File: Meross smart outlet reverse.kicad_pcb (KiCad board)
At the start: 2 copper layers, 60 x 33 mm, 61 parts, among them CN1 Conn_01x01, CN2 Conn_01x01, K1 HF32FV-16/5-HLTF(590), Q1 MMBT3904, SW1 SW_SPST, U1 OB2222M, U2 STK17-3.3, U3 CSE7759B

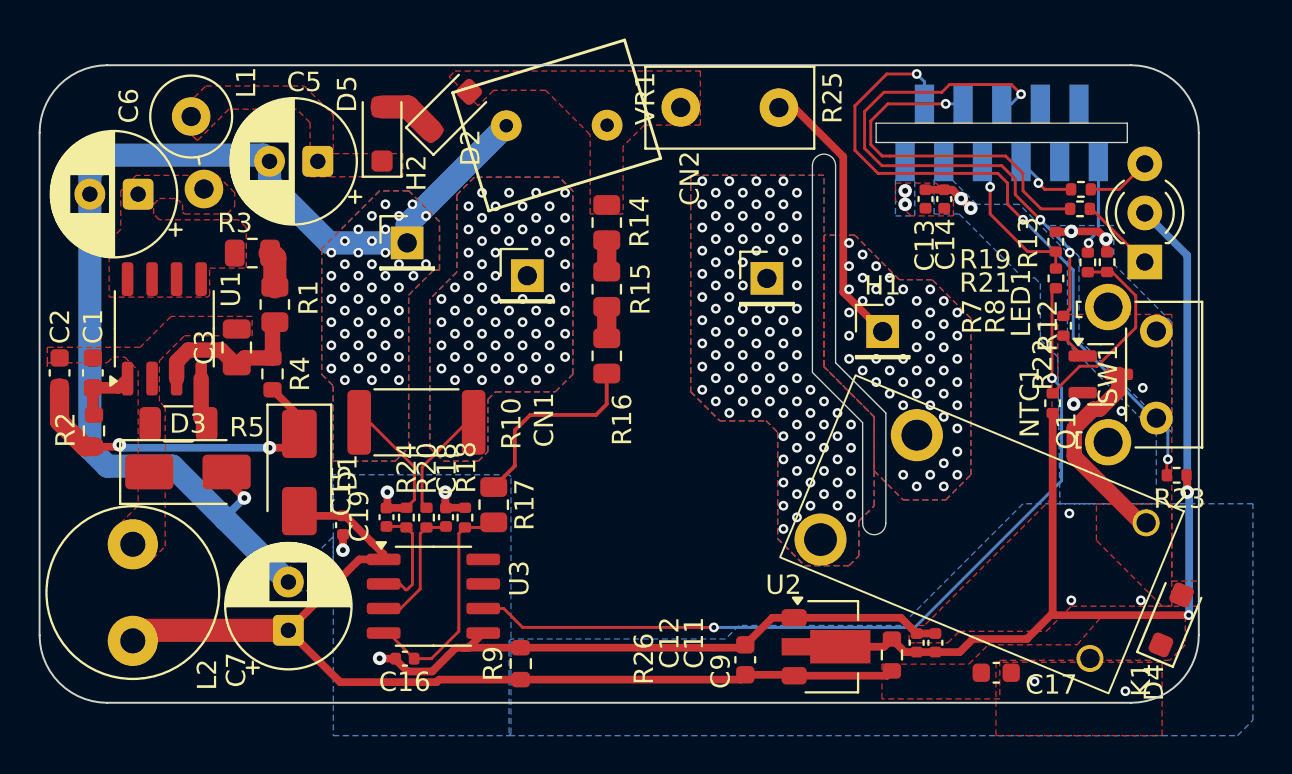
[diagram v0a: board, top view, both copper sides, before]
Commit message: Fixed plug and receptacle foots. No components left to fix but L1? And the silk and fab layers. And some kind of labeling of the design.
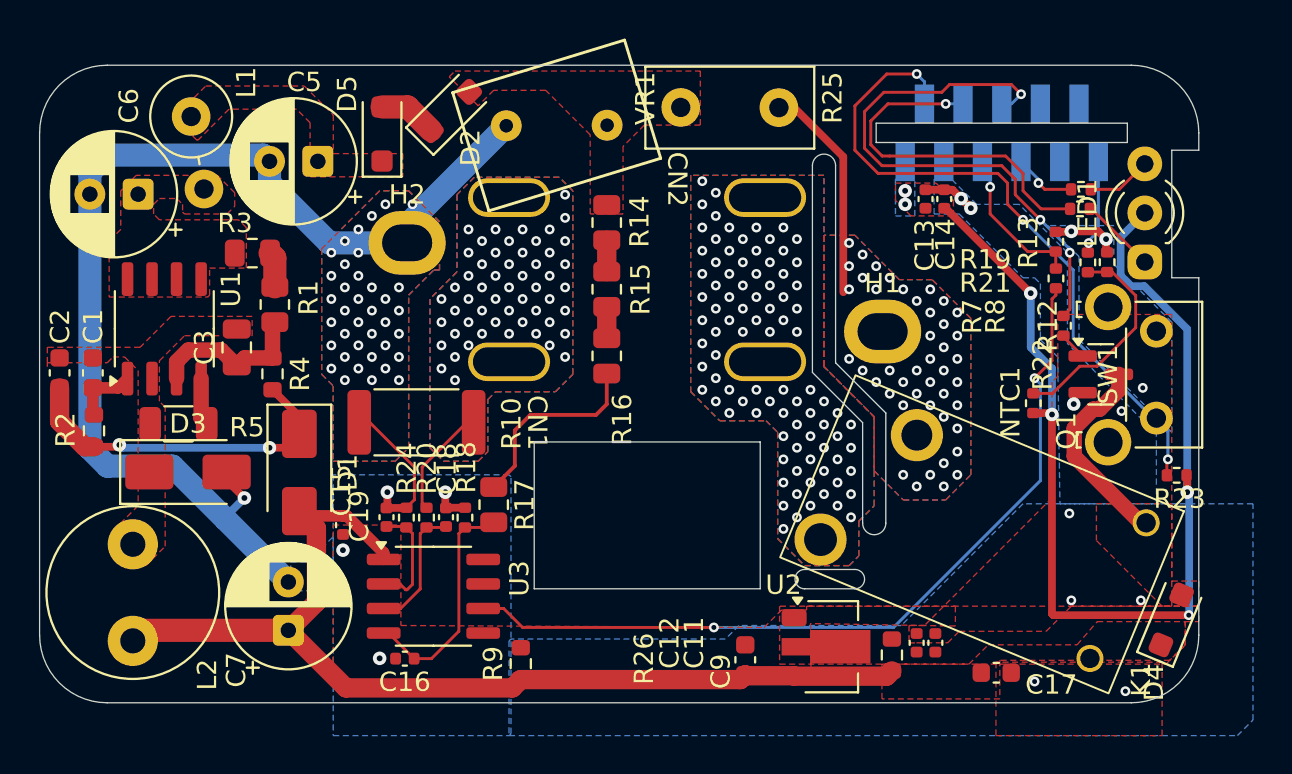
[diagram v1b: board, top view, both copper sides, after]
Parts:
- C11: value 3.3µF -> 10µF
- C12: value 100nF -> 10µF
- C13, C14: value C -> 10µF
- C15: value 100nF -> 1µF
- CN1, CN2: footprint Connector_PinHeader_2.54mm:PinHeader_1x01_P2.54mm_Vertical -> HF relays:NEMA5R_blade
- H1, H2: footprint Connector_PinHeader_2.54mm:PinHeader_1x01_P2.54mm_Vertical -> HF relays:NEMA5P_post
- L1: value L -> 2.2mH
- LED1: value LED_Dual_KAK -> LED_Dual_RG; footprint LED_THT:LED_D3.0mm-3 -> HF relays:LED_D3.0mm-3_Horiz
- moved NTC1 1.00 mm to (173.4, 101.0)
- moved CN1 0.97 mm to (146.3, 94.6), turned to -90 degrees
- moved CN2 0.12 mm to (159.6, 94.6), turned to -90 degrees
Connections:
- net /Power Supplies/HV_DC renamed /power supplies/HV_DC
- net /Power Supplies/RECT_AC renamed /power supplies/RECT_AC
- net /Power Supplies/U1_GND renamed /power supplies/U1_GND
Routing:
- net NEUTRAL_SRC: track 106.9 -> 74.2 mm, vias 64 -> 54
- net LINE_IN: track 14.3 -> 11.4 mm, vias 52 -> 44
- net Net-(NTC1-Pad1): track 10.4 -> 11.4 mm
- net +5V: track 53.1 -> 54.0 mm
- net +3V3: track 54.9 -> 55.8 mm, vias 4 -> 6
- net /current measurement/MEAS_SER_5V: track 43.7 -> 42.9 mm
- net NEUTRAL_LOAD: vias 69 -> 54
- net LINE_OUT: vias 108 -> 90
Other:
- outline, holes or cut-outs redrawn

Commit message: Fixed silk, fixed fab. Fixed a few part 3D models. Starting to rename stuff.
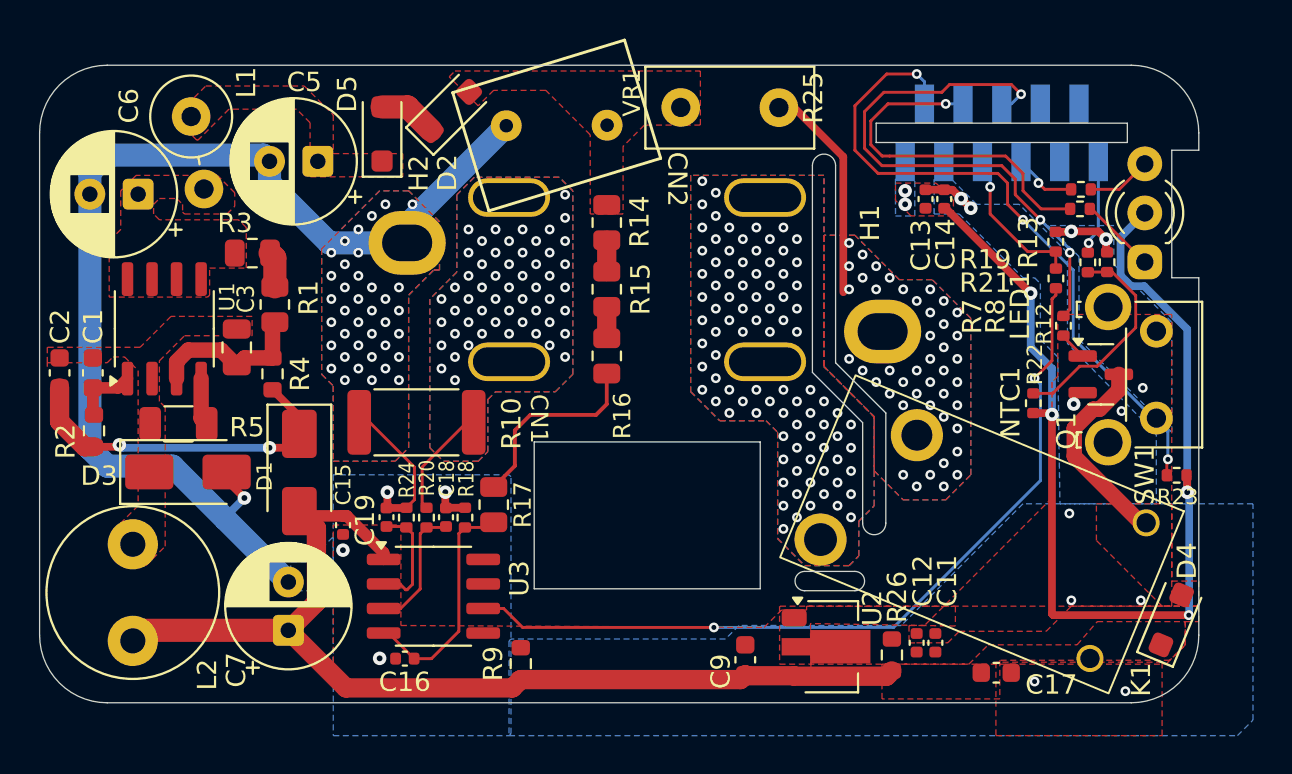
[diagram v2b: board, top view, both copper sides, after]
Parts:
- SW1: value SW_SPST -> B3F-3120
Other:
- outline, holes or cut-outs redrawn
